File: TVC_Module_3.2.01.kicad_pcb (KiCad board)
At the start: 4 copper layers, 96 x 96 mm, 67 parts, among them CN1 5051102091, CN2 505110-1192, J1 Conn_01x02_Male, J2 1720640012, J3 1720640012, J4 Conn_02x08_Odd_Even, J5 Conn_02x08_Odd_Even, J6 1720640012, Q1 FDS9926A, Q2 FDS9926A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

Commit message: Added GND vias
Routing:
- net GND: vias 428 -> 449

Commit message: Added more GND vias
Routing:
- net GND: vias 449 -> 452
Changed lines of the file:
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@@
   (via (at 165.25 114.75) (size 0.8) (drill 0.4) (layers "F.Cu" "B.Cu") (free) (net 3))
   (via (at 192.5 135) (size 0.8) (drill 0.4) (layers "F.Cu" "B.Cu") (free) (net 3))
-  (via (at 132.5 112.5) (size 0.8) (drill 0.4) (layers "F.Cu" "B.Cu") (free) (net 3))
+  (via (at 132.5 112.75) (size 0.8) (drill 0.4) (layers "F.Cu" "B.Cu") (free) (net 3))
   (via (at 164.75 94) (size 0.8) (drill 0.4) (layers "F.Cu" "B.Cu") (free) (net 3))
   (via (at 145 97.5) (size 0.8) (drill 0.4) (layers "F.Cu" "B.Cu") (free) (net 3))
@@
   (via (at 190 60) (size 0.8) (drill 0.4) (layers "F.Cu" "B.Cu") (free) (net 3))
   (via (at 190 57.5) (size 0.8) (drill 0.4) (layers "F.Cu" "B.Cu") (free) (net 3))
+  (via (at 130 115) (size 0.8) (drill 0.4) (layers "F.Cu" "B.Cu") (free) (net 3))
   (via (at 122.5 52.4) (size 0.8) (drill 0.4) (layers "F.Cu" "B.Cu") (free) (net 3))
   (via (at 177.5 52.5) (size 0.8) (drill 0.4) (layers "F.Cu" "B.Cu") (free) (net 3))
@@
   (via (at 147.5 142.5) (size 0.8) (drill 0.4) (layers "F.Cu" "B.Cu") (free) (net 3))
   (via (at 177.5 50) (size 0.8) (drill 0.4) (layers "F.Cu" "B.Cu") (free) (net 3))
+  (via (at 130 117.5) (size 0.8) (drill 0.4) (layers "F.Cu" "B.Cu") (free) (net 3))
   (via (at 195 122.5) (size 0.8) (drill 0.4) (layers "F.Cu" "B.Cu") (free) (net 3))
   (via (at 127.75 52.4) (size 0.8) (drill 0.4) (layers "F.Cu" "B.Cu") (free) (net 3))
@@
   (via (at 125 53.65) (size 0.8) (drill 0.4) (layers "F.Cu" "B.Cu") (free) (net 3))
   (via (at 121.25 53.65) (size 0.8) (drill 0.4) (layers "F.Cu" "B.Cu") (free) (net 3))
+  (via (at 130 120) (size 0.8) (drill 0.4) (layers "F.Cu" "B.Cu") (free) (net 3))
   (via (at 184.65 64.175) (size 0.45) (drill 0.3) (layers "F.Cu" "B.Cu") (free) (net 3))
   (via (at 152.5 105) (size 0.8) (drill 0.4) (layers "F.Cu" "B.Cu") (free) (net 3))

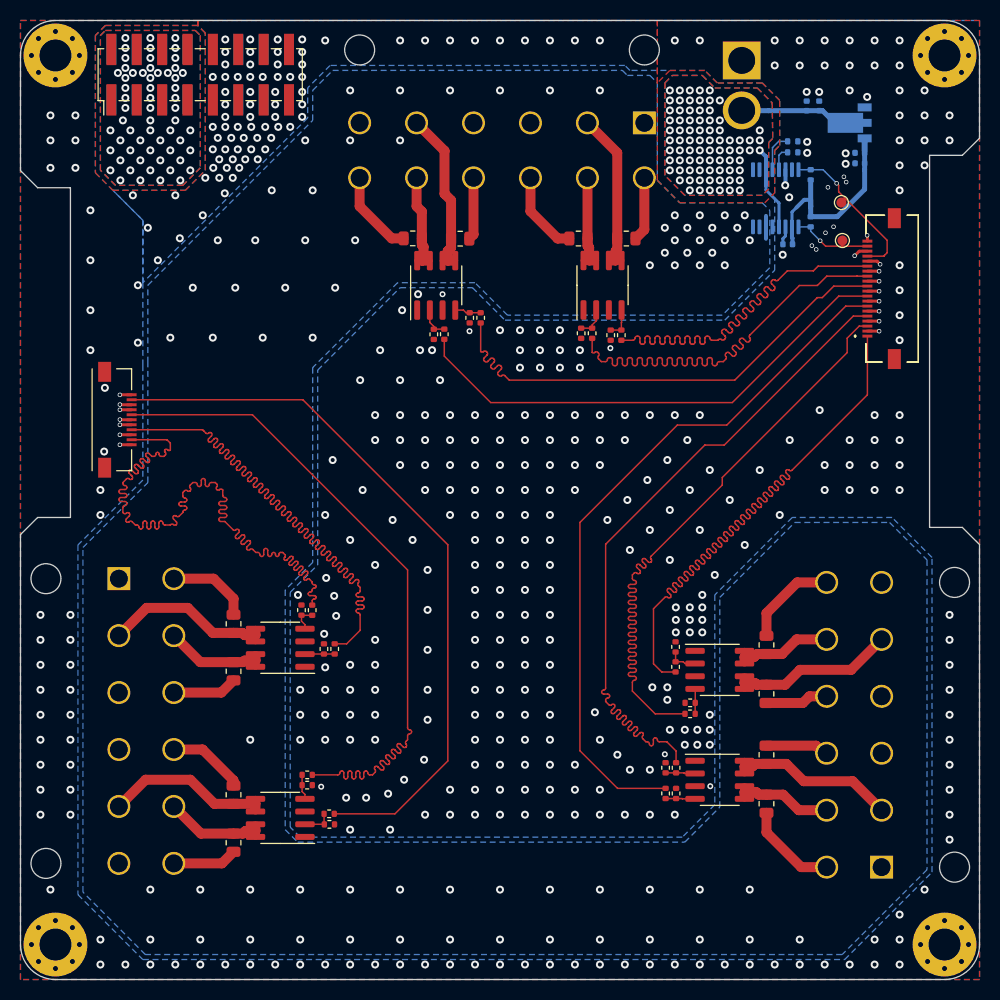
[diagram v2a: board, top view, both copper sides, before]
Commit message: Changed PWR I2C address
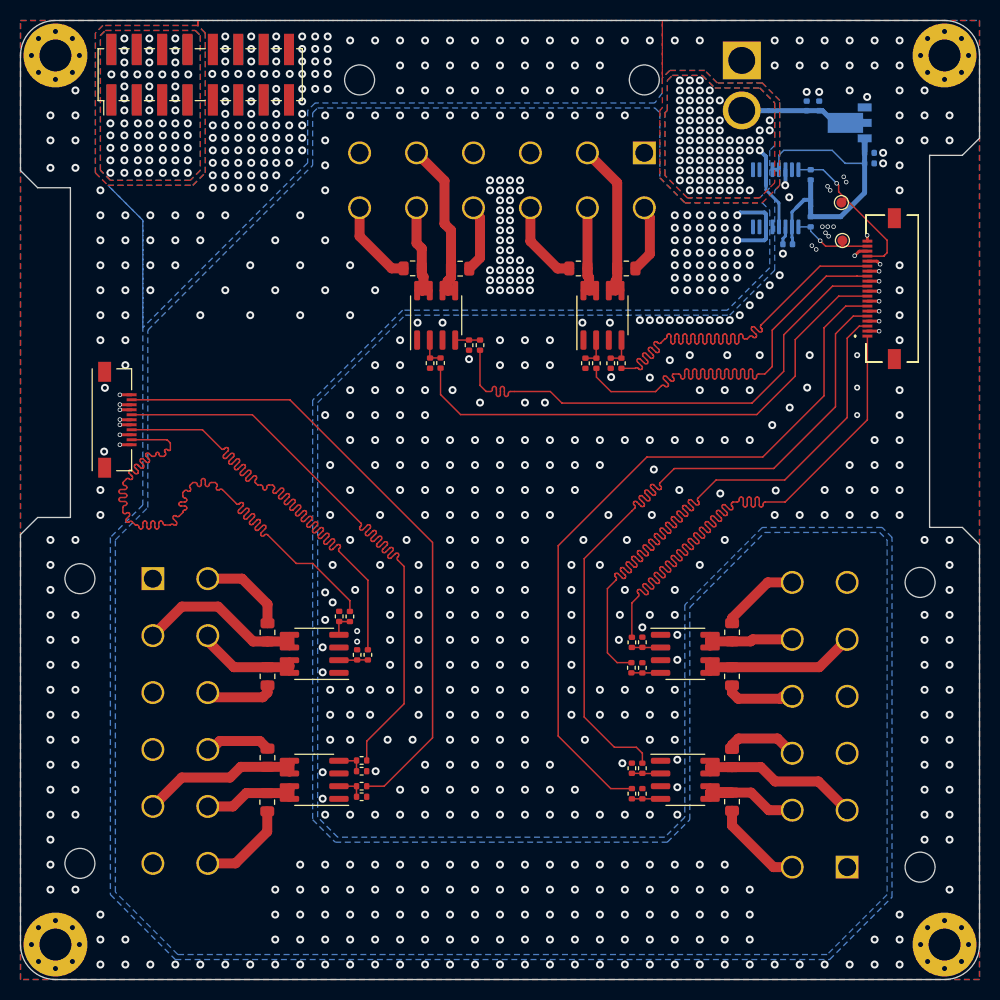
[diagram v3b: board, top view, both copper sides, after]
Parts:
- removed R37, R38: 10K, Resistor_SMD:R_0402_1005Metric
- moved R13 7.47 mm to (163.2, 112.8), turned to -90 degrees
- moved R15 5.93 mm to (164.2, 112.8), turned to 90 degrees
- moved R26 5.64 mm to (136.2, 122.1)
- moved R28 5.62 mm to (136.2, 123.2)
- moved R29 5.27 mm to (126.7, 126.2)
- moved Q5 5.11 mm to (131.4, 124.0)
- moved R30 5.03 mm to (126.7, 121.8)
- moved R14 5.02 mm to (163.2, 110.2), turned to -90 degrees
- moved R25 4.27 mm to (136.2, 124.7)
- moved R27 4.25 mm to (136.2, 125.7)
- moved R17 3.88 mm to (173.2, 113.7)
- moved R34 3.82 mm to (133.9, 107.7)
- moved R32 3.82 mm to (135.0, 107.7)
- moved Q3 3.81 mm to (168.6, 111.4)
- moved R18 3.67 mm to (173.2, 109.2)
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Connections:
- U2 pad 4: Net-(R37-Pad1) -> +3.3V
- U2 pad 5: Net-(R38-Pad1) -> +3.3V
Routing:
- net +3.3V: track 21.6 -> 33.3 mm
- net +6.8V: track 92.7 -> 102.7 mm, vias 70 -> 189
- net FLI_PWM_4_TIM2_CH4: track 72.9 -> 64.2 mm
- net FLI_PWM_3_TIM2_CH3: track 72.5 -> 64.1 mm
- net FLI_PWM_1_TIM5_CH1: track 72.1 -> 63.9 mm
- net FLI_PWM_2_TIM2_CH2: track 79.3 -> 72.3 mm
- net FLI_PWM_5_TIM2_CH1: track 46.3 -> 52.7 mm
- net Net-(R37-Pad1): track 3.99 -> 0.00 mm
- net FLI_PWM_12_TIM1_CH4: track 50.1 -> 53.0 mm
- net FLI_PWM_11_TIM3_CH3: track 50.1 -> 53.1 mm
- net FLI_PWM_10_TIM3_CH2: track 50.4 -> 53.3 mm
- net FLI_PWM_8_TIM4_CH4: track 70.3 -> 73.2 mm
- net FLI_PWM_9_TIM3_CH1: track 70.7 -> 73.5 mm
- net FLI_PWM_6_TIM4_CH2: track 71.0 -> 73.5 mm
- net Net-(R38-Pad1): track 2.44 -> 0.00 mm
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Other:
- board text removed: "JLCJLCJLCJLC"

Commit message: Corrected power planes
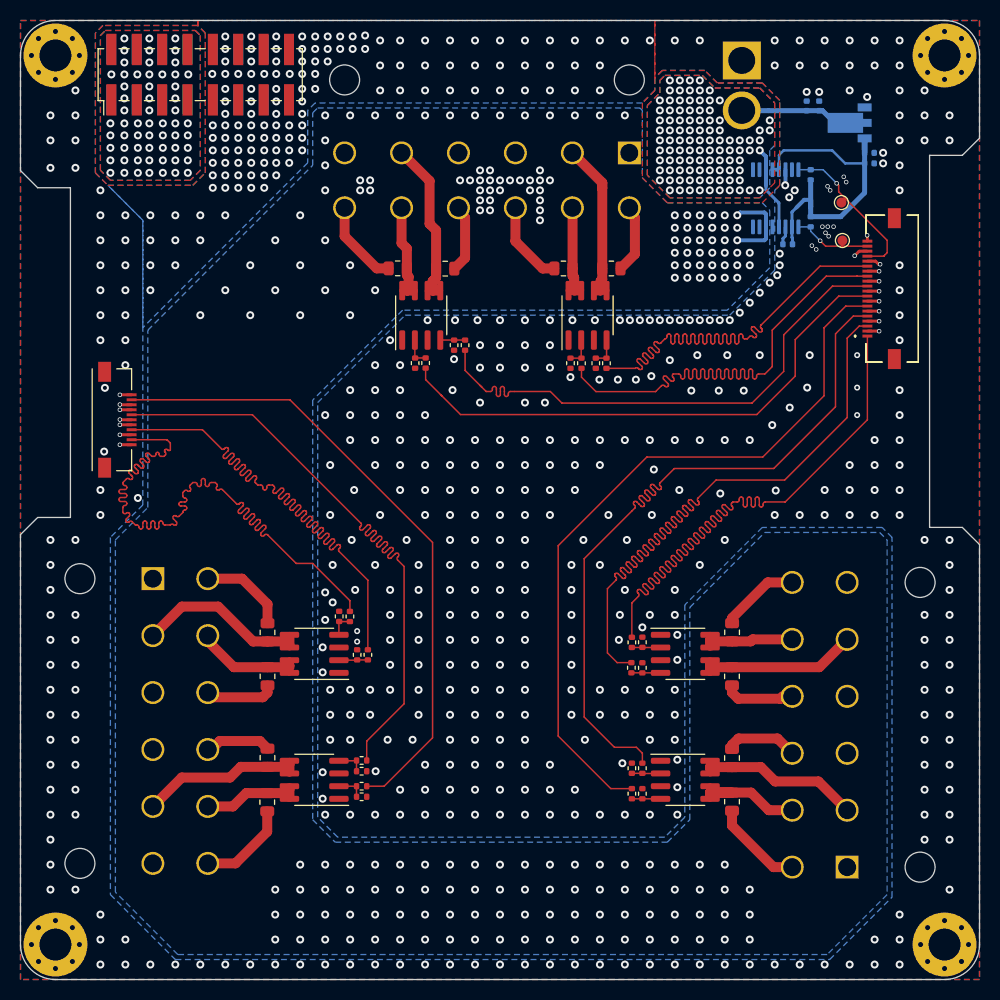
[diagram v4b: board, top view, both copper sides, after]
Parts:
- moved J2 1.50 mm to (162.9, 61.2)
- moved Q1 1.50 mm to (142.1, 77.5)
- moved R1 1.50 mm to (146.5, 80.5)
- moved R10 1.50 mm to (159.6, 82.3)
- moved R11 1.50 mm to (156.3, 72.8)
- moved R12 1.50 mm to (161.1, 72.8)
- moved R2 1.50 mm to (142.6, 82.3)
- moved R3 1.50 mm to (145.4, 80.5)
- moved R4 1.50 mm to (141.5, 82.3)
- moved R5 1.50 mm to (139.8, 72.8)
- moved R6 1.50 mm to (144.5, 72.8)
- moved R7 1.50 mm to (158.2, 82.3)
- moved R8 1.50 mm to (160.7, 82.3)
- moved R9 1.50 mm to (157.1, 82.3)
- moved Q2 1.49 mm to (158.8, 77.5)
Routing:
- net FLI_PWM_12_TIM1_CH4: track 53.0 -> 54.5 mm
- net FLI_PWM_5_TIM2_CH1: track 52.7 -> 54.2 mm
- net FLI_PWM_10_TIM3_CH2: track 53.3 -> 54.1 mm
- net FLI_PWM_11_TIM3_CH3: track 53.1 -> 53.9 mm
- net SERVO_3: track 16.3 -> 16.9 mm
- net +6.8V: track 102.7 -> 103.2 mm, vias 189 -> 175
- net TVC_IN: vias 75 -> 98
- net GND: vias 568 -> 586
